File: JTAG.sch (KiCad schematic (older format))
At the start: 55 parts, among them CN5 CONN_RCPT_USB2.0_MINI_B_SMD_R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, U15 FT2232HL-REEL, X2 ABM3B-12.000MHZ

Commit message: Annotation has been done
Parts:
- gave numbers to parts that had none: 30

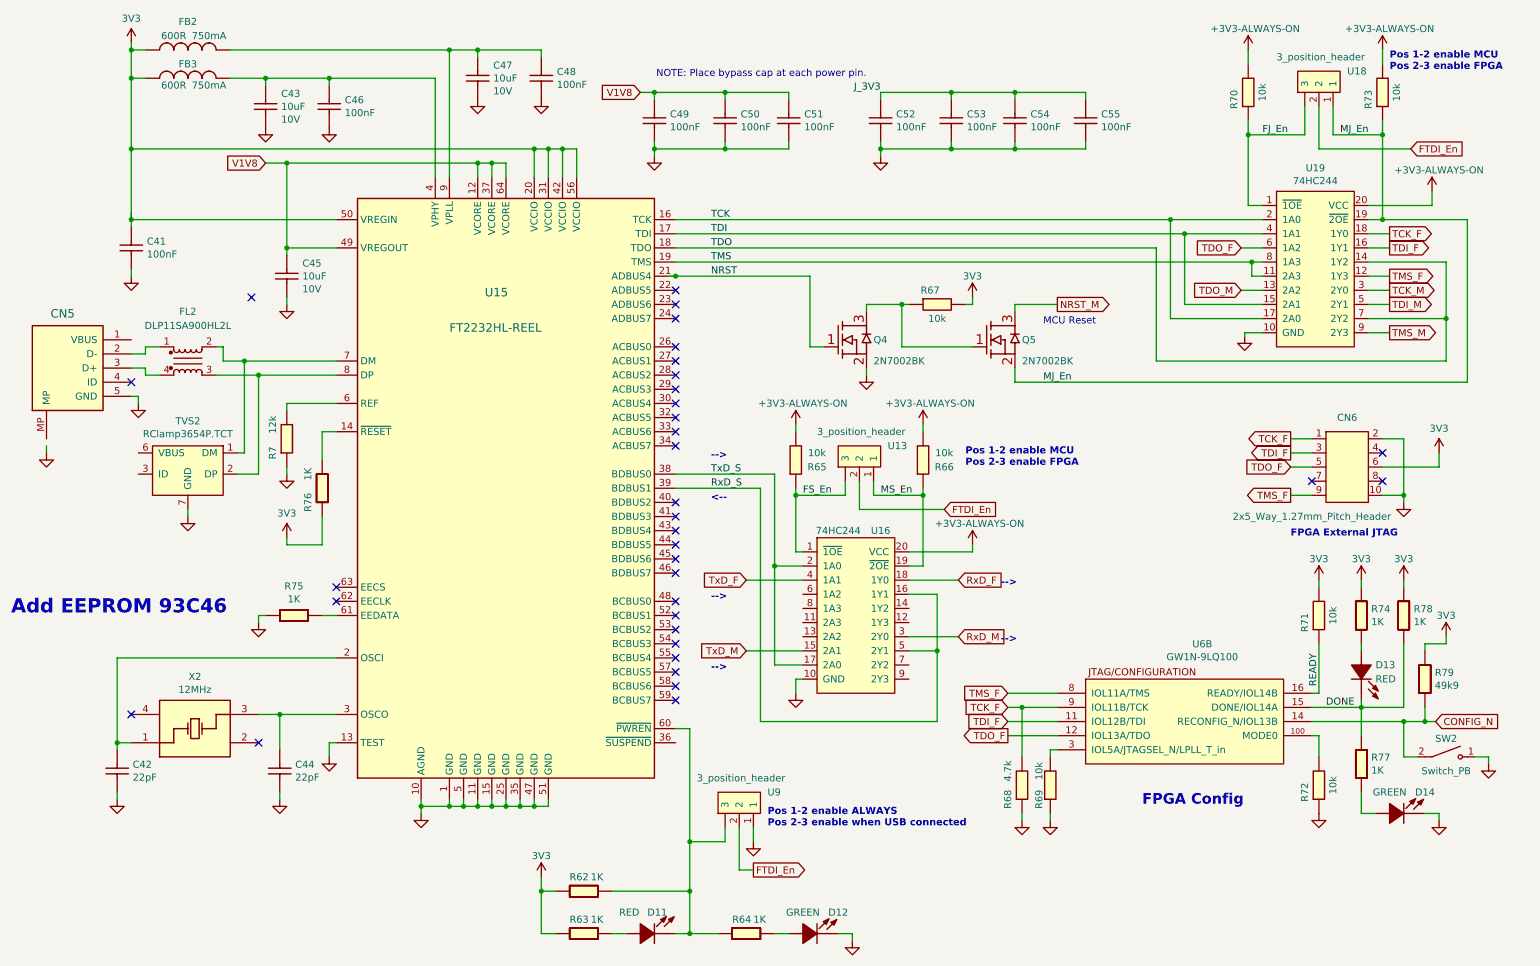
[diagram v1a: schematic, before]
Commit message: Output BOM. Swapped some resistors to match text value
R68 was 12k symbol but 4k7 text, changed to 4k7 symbol. R71, R69, R70, R73, R67, R65 were 12k symbol but 10k text, swapped to 10 symbol.
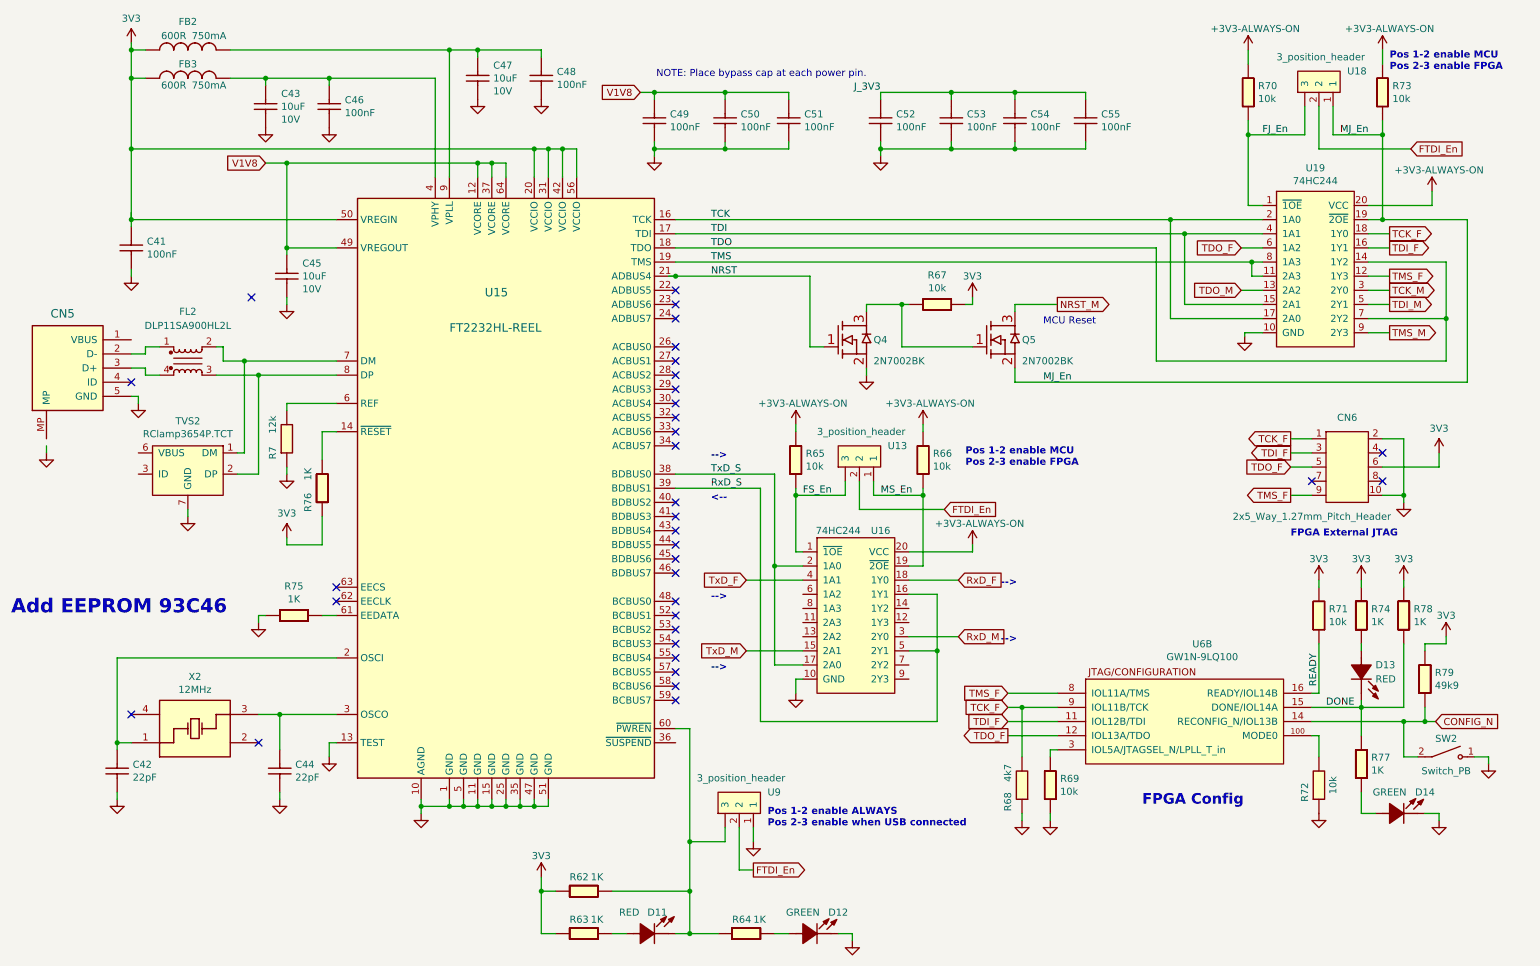
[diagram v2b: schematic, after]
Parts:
- removed R65, R66, R67, R68, R69, R70, R71, R73: 12k_0603_Chip_Resistor,_1%,_0.1W, Resistor_SMD:R_0603_1608Metric, symbol OpenVent:12k_0603_Chip_Resistor,_1%,_0.1W
- added R65, R66, R67, R69, R70, R71, R73: 10k_0603_Chip_Resistor,_1%,_0.1W, symbol OpenVent:10k_0603_Chip_Resistor,_1%,_0.1W
- added R68: 4k7_0603_Chip_Resistor,_1%,_0.1W, symbol OpenVent:4k7_0603_Chip_Resistor,_1%,_0.1W
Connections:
- net +3V3: now also R67.2, R71.1
- net FJ_En: now also R70.2
- net FS_En: now also R65.2
- net GND: now also R68.1, R69.2
- net MJ_En: now also R73.2
- net MS_En: now also R66.2
- net READY: now also R71.2
- net TCK_F: now also R68.2
- net VDC: now also R65.1, R66.1, R70.1, R73.1
- net at U6.3 (IOL5A/JTAGSEL_N/LPLL_T_in): now also R69.1
- net at Q4.3 (D), Q5.1 (G1): now also R67.1
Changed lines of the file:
@@
 	1    0    0    -1
-$EndComp
-$Comp
-L OpenVent:12k_0603_Chip_Resistor,_1%,_0.1W R68
-U 1 1 6073BA6B
-P 7600 6200
-AR Path="/5F8F8987/6073BA6B" Ref="R68"  Part="1"
-AR Path="/5FB692C4/6073BA6B" Ref="R?"  Part="1"
-AR Path="/5FBE8499/6073BA6B" Ref="R?"  Part="1"
-F 0 "R68" H 7600 6200 50  0000 C CNN
-F 1 "12k_0603_Chip_Resistor,_1%,_0.1W" H 7600 6200 50  0001 C CNN
-F 2 "Resistor_SMD:R_0603_1608Metric" H 7600 6200 50  0001 C CNN
-F 3 "" H 7600 6200 50  0001 C CNN
-F 4 "4.7k" H 7800 6200 50  0000 C CNN "Val"
-F 5 "1%" H 7600 6200 50  0001 C CNN "Tolerance"
-F 6 "0.1W" H 7600 6200 50  0001 C CNN "Watt"
-	1    7600 6200
-	0    -1   -1   0
 $EndComp
 Wire Wire Line
@@
 Text Label 9850 5550 0    50   ~ 0
 DONE
-$Comp
-L OpenVent:12k_0603_Chip_Resistor,_1%,_0.1W R71
-U 1 1 6073BAB6
-P 9700 5000
-AR Path="/5F8F8987/6073BAB6" Ref="R71"  Part="1"
-AR Path="/5FB692C4/6073BAB6" Ref="R?"  Part="1"
-AR Path="/5FBE8499/6073BAB6" Ref="R?"  Part="1"
-F 0 "R71" H 9750 5000 50  0000 C CNN
-F 1 "12k_0603_Chip_Resistor,_1%,_0.1W" H 9700 5000 50  0001 C CNN
-F 2 "Resistor_SMD:R_0603_1608Metric" H 9700 5000 50  0001 C CNN
-F 3 "" H 9700 5000 50  0001 C CNN
-F 4 "10k" H 9800 4800 50  0000 C CNN "Val"
-F 5 "1%" H 9700 5000 50  0001 C CNN "Tolerance"
-F 6 "0.1W" H 9700 5000 50  0001 C CNN "Watt"
-	1    9700 5000
-	0    -1   -1   0
-$EndComp
 Wire Wire Line
 	9750 5450 9800 5450
@@
 	1    7900 6350
 	1    0    0    -1
-$EndComp
-$Comp
-L OpenVent:12k_0603_Chip_Resistor,_1%,_0.1W R69
-U 1 1 6073BAE7
-P 7800 6200
-AR Path="/5F8F8987/6073BAE7" Ref="R69"  Part="1"
-AR Path="/5FB692C4/6073BAE7" Ref="R?"  Part="1"
-AR Path="/5FBE8499/6073BAE7" Ref="R?"  Part="1"
-F 0 "R69" H 7800 6150 50  0000 C BNN
-F 1 "12k_0603_Chip_Resistor,_1%,_0.1W" H 7800 6200 50  0001 C CNN
-F 2 "Resistor_SMD:R_0603_1608Metric" H 7800 6200 50  0001 C CNN
-F 3 "" H 7800 6200 50  0001 C CNN
-F 4 "10k" H 8000 6150 50  0000 C BNN "Val"
-F 5 "1%" H 7800 6200 50  0001 C CNN "Tolerance"
-F 6 "0.1W" H 7800 6200 50  0001 C CNN "Watt"
-	1    7800 6200
-	0    -1   -1   0
 $EndComp
 Wire Wire Line
@@
 Wire Wire Line
 	9700 1500 9700 1300
-$Comp
-L OpenVent:12k_0603_Chip_Resistor,_1%,_0.1W R70
-U 1 1 60A9E36F
-P 9200 1300
-AR Path="/5F8F8987/60A9E36F" Ref="R70"  Part="1"
-AR Path="/5FB692C4/60A9E36F" Ref="R?"  Part="1"
-AR Path="/5FBE8499/60A9E36F" Ref="R?"  Part="1"
-F 0 "R70" H 9250 1300 50  0000 C CNN
-F 1 "12k_0603_Chip_Resistor,_1%,_0.1W" H 9200 1300 50  0001 C CNN
-F 2 "Resistor_SMD:R_0603_1608Metric" H 9200 1300 50  0001 C CNN
-F 3 "" H 9200 1300 50  0001 C CNN
-F 4 "10k" H 9300 1100 50  0000 C CNN "Val"
-F 5 "1%" H 9200 1300 50  0001 C CNN "Tolerance"
-F 6 "0.1W" H 9200 1300 50  0001 C CNN "Watt"
-	1    9200 1300
-	0    -1   -1   0
-$EndComp
 Wire Wire Line
 	9300 1400 9300 1500
@@
 Wire Wire Line
 	10250 900  10250 1000
-$Comp
-L OpenVent:12k_0603_Chip_Resistor,_1%,_0.1W R73
-U 1 1 60AFBDEA
-P 10150 1300
-AR Path="/5F8F8987/60AFBDEA" Ref="R73"  Part="1"
-AR Path="/5FB692C4/60AFBDEA" Ref="R?"  Part="1"
-AR Path="/5FBE8499/60AFBDEA" Ref="R?"  Part="1"
-F 0 "R73" H 10200 1300 50  0000 C CNN
-F 1 "12k_0603_Chip_Resistor,_1%,_0.1W" H 10150 1300 50  0001 C CNN
-F 2 "Resistor_SMD:R_0603_1608Metric" H 10150 1300 50  0001 C CNN
-F 3 "" H 10150 1300 50  0001 C CNN
-F 4 "10k" H 10250 1100 50  0000 C CNN "Val"
-F 5 "1%" H 10150 1300 50  0001 C CNN "Tolerance"
-F 6 "0.1W" H 10150 1300 50  0001 C CNN "Watt"
-	1    10150 1300
-	0    -1   -1   0
-$EndComp
 Wire Wire Line
 	10250 1400 10250 1500
@@
 Wire Wire Line
 	7300 2700 7350 2700
-$Comp
-L OpenVent:12k_0603_Chip_Resistor,_1%,_0.1W R67
-U 1 1 60997889
-P 7000 2600
-AR Path="/5F8F8987/60997889" Ref="R67"  Part="1"
-AR Path="/5FB692C4/60997889" Ref="R?"  Part="1"
-AR Path="/5FBE8499/60997889" Ref="R?"  Part="1"
-F 0 "R67" H 7050 2600 50  0000 C CNN
-F 1 "12k_0603_Chip_Resistor,_1%,_0.1W" H 7000 2600 50  0001 C CNN
-F 2 "Resistor_SMD:R_0603_1608Metric" H 7000 2600 50  0001 C CNN
-F 3 "" H 7000 2600 50  0001 C CNN
-F 4 "10k" H 7100 2400 50  0000 C CNN "Val"
-F 5 "1%" H 7000 2600 50  0001 C CNN "Tolerance"
-F 6 "0.1W" H 7000 2600 50  0001 C CNN "Watt"
-	1    7000 2600
-	1    0    0    -1
-$EndComp
 Wire Wire Line
 	5250 2400 9325 2400
@@
 Wire Wire Line
 	6450 4050 6450 3950
-$Comp
-L OpenVent:12k_0603_Chip_Resistor,_1%,_0.1W R65
-U 1 1 6317ACC3
-P 6000 3900
-AR Path="/5F8F8987/6317ACC3" Ref="R65"  Part="1"
-AR Path="/5FB692C4/6317ACC3" Ref="R?"  Part="1"
-AR Path="/5FBE8499/6317ACC3" Ref="R?"  Part="1"
-F 0 "R65" V 6050 3650 50  0000 C CNN
-F 1 "12k_0603_Chip_Resistor,_1%,_0.1W" H 6000 3900 50  0001 C CNN
-F 2 "Resistor_SMD:R_0603_1608Metric" H 6000 3900 50  0001 C CNN
-F 3 "" H 6000 3900 50  0001 C CNN
-F 4 "10k" V 6150 3650 50  0000 C CNN "Val"
-F 5 "1%" H 6000 3900 50  0001 C CNN "Tolerance"
-F 6 "0.1W" H 6000 3900 50  0001 C CNN "Watt"
-	1    6000 3900
-	0    -1   -1   0
-$EndComp
 Wire Wire Line
 	6100 4000 6100 4050
@@
 Wire Wire Line
 	7000 3550 7000 3600
-$Comp
-L OpenVent:12k_0603_Chip_Resistor,_1%,_0.1W R66
-U 1 1 6317ACD2
-P 6900 3900
-AR Path="/5F8F8987/6317ACD2" Ref="R66"  Part="1"
-AR Path="/5FB692C4/6317ACD2" Ref="R?"  Part="1"
-AR Path="/5FBE8499/6317ACD2" Ref="R?"  Part="1"
-F 0 "R66" V 6950 3650 50  0000 C CNN
-F 1 "12k_0603_Chip_Resistor,_1%,_0.1W" H 6900 3900 50  0001 C CNN
-F 2 "Resistor_SMD:R_0603_1608Metric" H 6900 3900 50  0001 C CNN
-F 3 "" H 6900 3900 50  0001 C CNN
-F 4 "10k" V 7050 3650 50  0000 C CNN "Val"
-F 5 "1%" H 6900 3900 50  0001 C CNN "Tolerance"
-F 6 "0.1W" H 6900 3900 50  0001 C CNN "Watt"
-	1    6900 3900
-	0    -1   -1   0
-$EndComp
 Wire Wire Line
 	7000 4000 7000 4050
@@
 Text GLabel 7950 2700 2    50   Output ~ 0
 NRST_M
+$Comp
+L OpenVent:4k7_0603_Chip_Resistor,_1%,_0.1W R68
+U 1 1 60896609
+P 7600 6200
+F 0 "R68" H 7550 6200 50  0000 L CNN
+F 1 "4k7_0603_Chip_Resistor,_1%,_0.1W" H 7600 6200 50  0001 C CNN
+F 2 "" H 7600 6200 50  0001 C CNN
+F 3 "" H 7600 6200 60  0001 C CNN
+F 4 "4k7" H 7350 6200 50  0000 L CNN "Val"
+F 5 "1%" H 7600 6200 50  0001 C CNN "Tolerance"
+F 6 "0.1W" H 7600 6200 50  0001 C CNN "Watt"
+	1    7600 6200
+	0    1    1    0
+$EndComp
+$Comp
+L OpenVent:10k_0603_Chip_Resistor,_1%,_0.1W R71
+U 1 1 608DD9C5
+P 9900 4800
+F 0 "R71" V 9954 4770 50  0000 L CNN
+F 1 "10k_0603_Chip_Resistor,_1%,_0.1W" H 9900 4800 50  0001 C CNN
+F 2 "" H 9900 4800 50  0001 C CNN
+F 3 "" H 9900 4800 50  0001 C CNN
+F 4 "10k" V 10045 4770 50  0000 L CNN "Val"
+F 5 "1%" H 9900 4800 50  0001 C CNN "Tolerance"
+F 6 "0.1W" H 9900 4800 50  0001 C CNN "Watt"
+	1    9900 4800
+	0    1    1    0
+$EndComp
+$Comp
+L OpenVent:10k_0603_Chip_Resistor,_1%,_0.1W R69
+U 1 1 60924674
+P 8000 6000
+F 0 "R69" V 8054 5970 50  0000 L CNN
+F 1 "10k_0603_Chip_Resistor,_1%,_0.1W" H 8000 6000 50  0001 C CNN
+F 2 "" H 8000 6000 50  0001 C CNN
+F 3 "" H 8000 6000 50  0001 C CNN
+F 4 "10k" V 8145 5970 50  0000 L CNN "Val"
+F 5 "1%" H 8000 6000 50  0001 C CNN "Tolerance"
+F 6 "0.1W" H 8000 6000 50  0001 C CNN "Watt"
+	1    8000 6000
+	0    1    1    0
+$EndComp
+$Comp
+L OpenVent:10k_0603_Chip_Resistor,_1%,_0.1W R70
+U 1 1 609B1077
+P 9400 1100
+F 0 "R70" V 9454 1070 50  0000 L CNN
+F 1 "10k_0603_Chip_Resistor,_1%,_0.1W" H 9400 1100 50  0001 C CNN
+F 2 "" H 9400 1100 50  0001 C CNN
+F 3 "" H 9400 1100 50  0001 C CNN
+F 4 "10k" V 9545 1070 50  0000 L CNN "Val"
+F 5 "1%" H 9400 1100 50  0001 C CNN "Tolerance"
+F 6 "0.1W" H 9400 1100 50  0001 C CNN "Watt"
+	1    9400 1100
+	0    1    1    0
+$EndComp
+$Comp
+L OpenVent:10k_0603_Chip_Resistor,_1%,_0.1W R73
+U 1 1 609F7B7A
+P 10350 1100
+F 0 "R73" V 10404 1070 50  0000 L CNN
+F 1 "10k_0603_Chip_Resistor,_1%,_0.1W" H 10350 1100 50  0001 C CNN
+F 2 "" H 10350 1100 50  0001 C CNN
+F 3 "" H 10350 1100 50  0001 C CNN
+F 4 "10k" V 10495 1070 50  0000 L CNN "Val"
+F 5 "1%" H 10350 1100 50  0001 C CNN "Tolerance"
+F 6 "0.1W" H 10350 1100 50  0001 C CNN "Watt"
+	1    10350 1100
+	0    1    1    0
+$EndComp
+$Comp
+L OpenVent:10k_0603_Chip_Resistor,_1%,_0.1W R67
+U 1 1 60A3D75F
+P 7000 2600
+F 0 "R67" H 7100 2707 50  0000 C CNN
+F 1 "10k_0603_Chip_Resistor,_1%,_0.1W" H 7000 2600 50  0001 C CNN
+F 2 "" H 7000 2600 50  0001 C CNN
+F 3 "" H 7000 2600 50  0001 C CNN
+F 4 "10k" H 7100 2616 50  0000 C CNN "Val"
+F 5 "1%" H 7000 2600 50  0001 C CNN "Tolerance"
+F 6 "0.1W" H 7000 2600 50  0001 C CNN "Watt"
+	1    7000 2600
+	1    0    0    -1
+$EndComp
+$Comp
+L OpenVent:10k_0603_Chip_Resistor,_1%,_0.1W R65
+U 1 1 60A6BD58
+P 6200 3700
+F 0 "R65" V 6254 3670 50  0000 L CNN
+F 1 "10k_0603_Chip_Resistor,_1%,_0.1W" H 6200 3700 50  0001 C CNN
+F 2 "" H 6200 3700 50  0001 C CNN
+F 3 "" H 6200 3700 50  0001 C CNN
+F 4 "10k" V 6345 3670 50  0000 L CNN "Val"
+F 5 "1%" H 6200 3700 50  0001 C CNN "Tolerance"
+F 6 "0.1W" H 6200 3700 50  0001 C CNN "Watt"
+	1    6200 3700
+	0    1    1    0
+$EndComp
+$Comp
+L OpenVent:10k_0603_Chip_Resistor,_1%,_0.1W R66
+U 1 1 60AC9168
+P 7100 3700
+F 0 "R66" V 7154 3670 50  0000 L CNN
+F 1 "10k_0603_Chip_Resistor,_1%,_0.1W" H 7100 3700 50  0001 C CNN
+F 2 "" H 7100 3700 50  0001 C CNN
+F 3 "" H 7100 3700 50  0001 C CNN
+F 4 "10k" V 7245 3670 50  0000 L CNN "Val"
+F 5 "1%" H 7100 3700 50  0001 C CNN "Tolerance"
+F 6 "0.1W" H 7100 3700 50  0001 C CNN "Watt"
+	1    7100 3700
+	0    1    1    0
+$EndComp
 $EndSCHEMATC

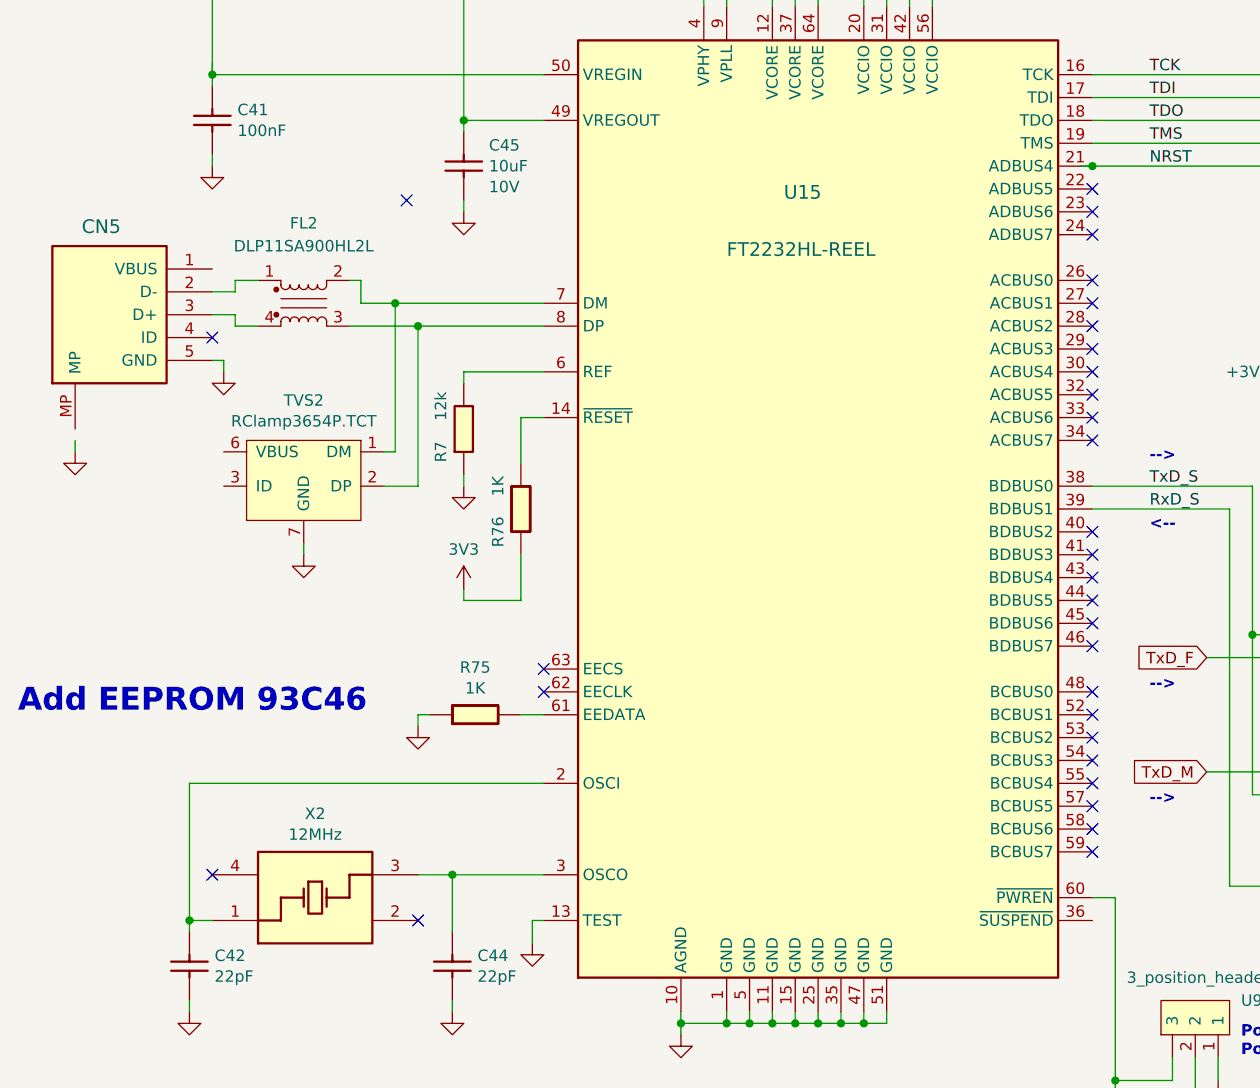
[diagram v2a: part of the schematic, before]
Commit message: Beginning the process of design review, fixed a couple howlers.
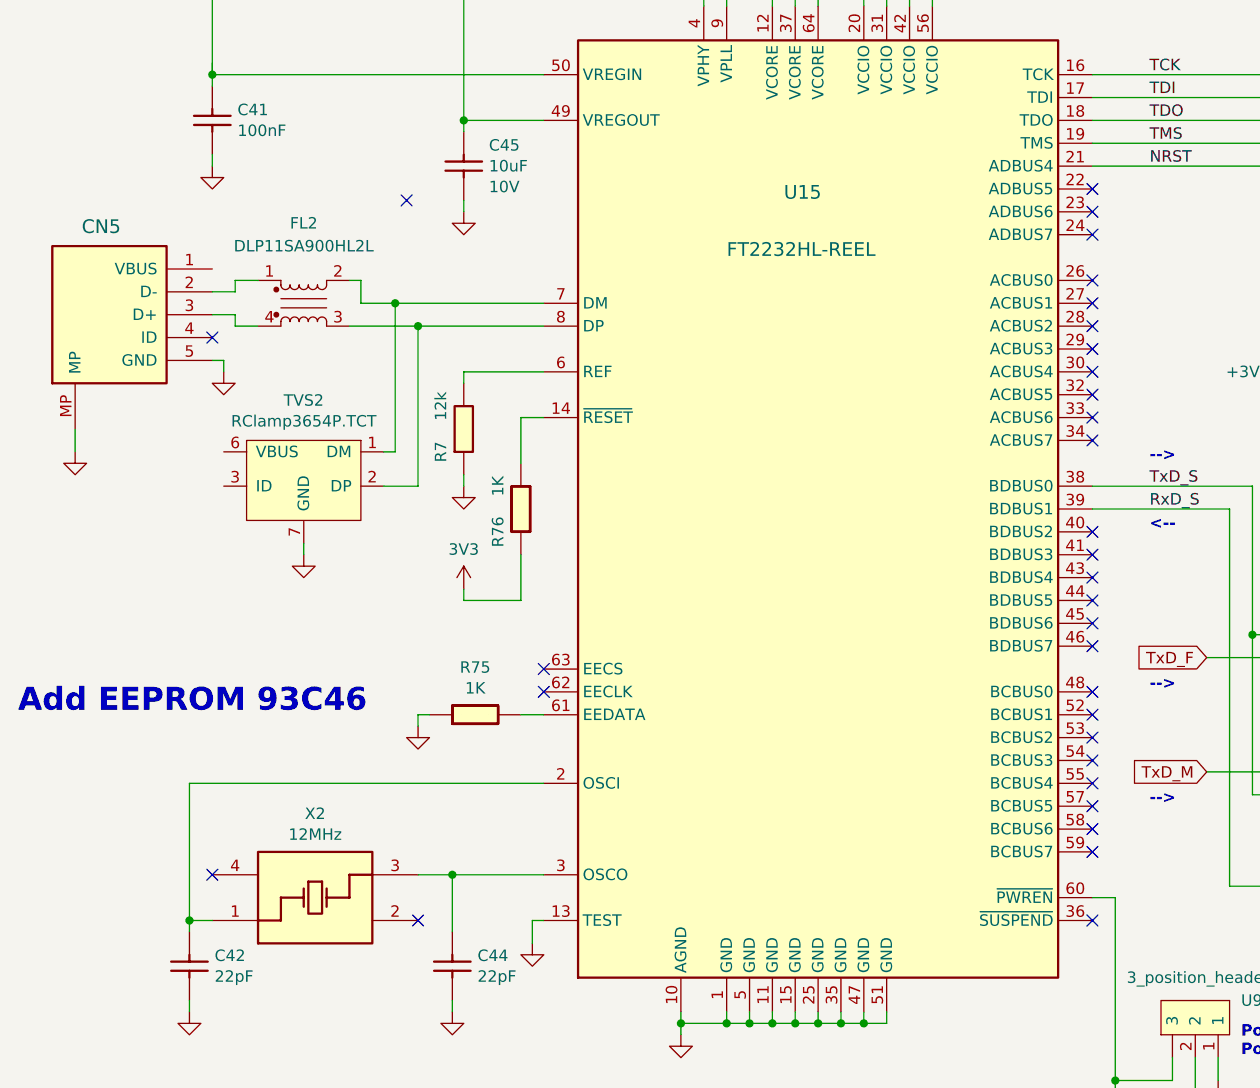
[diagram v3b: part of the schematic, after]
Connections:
- net GND: now also CN5.MP
- no-connect marks 34 -> 35
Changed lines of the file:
@@
 Wire Wire Line
 	10400 5650 10550 5650
-Wire Wire Line
-	800  3700 800  3750
 $Comp
 L OpenVent:74HC244 U19
@@
 	6200 2500 6200 3000
 Wire Wire Line
-	5200 2500 5250 2500
-Wire Wire Line
 	1400 2100 2850 2100
 Wire Wire Line
@@
 	6850 2700 6900 2700
 Connection ~ 6850 2700
-Connection ~ 5250 2500
 Wire Wire Line
 	5250 2500 6200 2500
@@
 	0    1    1    0
 $EndComp
+Wire Wire Line
+	800  3650 800  3750
+NoConn ~ 5250 5800
 $EndSCHEMATC
